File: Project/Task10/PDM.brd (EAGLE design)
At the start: 101.3 x 78.7 mm, 43 parts

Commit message: Final Board Revision
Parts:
- moved R1 6.35 mm to (73.7, 30.5)
- moved R2 6.35 mm to (73.7, 26.7)
- moved R3 6.35 mm to (73.7, 22.9)
- moved R4 6.35 mm to (73.7, 19.1)
- moved R5 6.35 mm to (73.7, 15.2)
- moved R6 6.35 mm to (73.7, 11.4)
- moved LED1 6.35 mm to (80.0, 30.5)
- moved LED2 6.35 mm to (80.0, 26.7)
- moved LED3 6.35 mm to (80.0, 22.9)
- moved LED4 6.35 mm to (80.0, 19.1)
- moved LED5 6.35 mm to (80.0, 15.2)
- moved LED6 6.35 mm to (80.0, 11.4)
- moved C9 1.27 mm to (82.5, 41.9)
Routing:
- net N$15: track 0.00 -> 71.0 mm, vias 0 -> 1
- net N$19: track 3.91 -> 66.0 mm, vias 0 -> 1
- net N$6: track 4.04 -> 57.6 mm, vias 0 -> 1
- net N$1: track 0.00 -> 51.6 mm, vias 0 -> 1
- net N$9: track 3.91 -> 55.5 mm, vias 0 -> 1
- net N$4: track 0.00 -> 42.2 mm, vias 0 -> 1
- net GND: track 36.3 -> 62.3 mm, vias 0 -> 3
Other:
- board size 101.3 x 78.7 mm -> 101.3 x 76.2 mm
- board text added: "Acc 1"
- board text added: "Acc 2"
- board text added: "Acc 3"
- board text added: "Arduino"
- board text added: "MRSD Team B, Fall 2013"
- board text added: "Power Status"
- board text added: "Rev 0.1"
- board text added: "Servo 1"
- board text added: "Servo 2"
- board text added: "Space Jockey Power Distribution Board"
- board text removed: "Power Distribution Board - Team Space Jockey"
- board text removed: "Status"

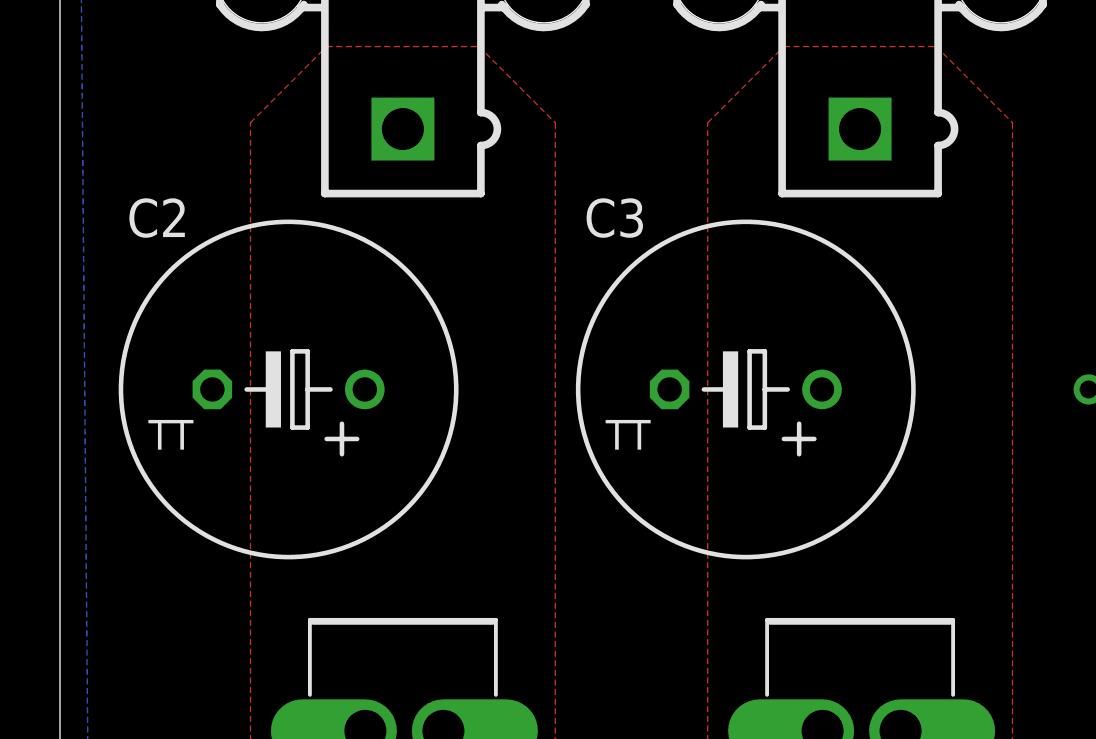
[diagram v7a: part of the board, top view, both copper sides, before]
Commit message: Final Board design.
Looks good. I just moved the giant capacitors one grid to the left to
enlarge the clearance with the ground
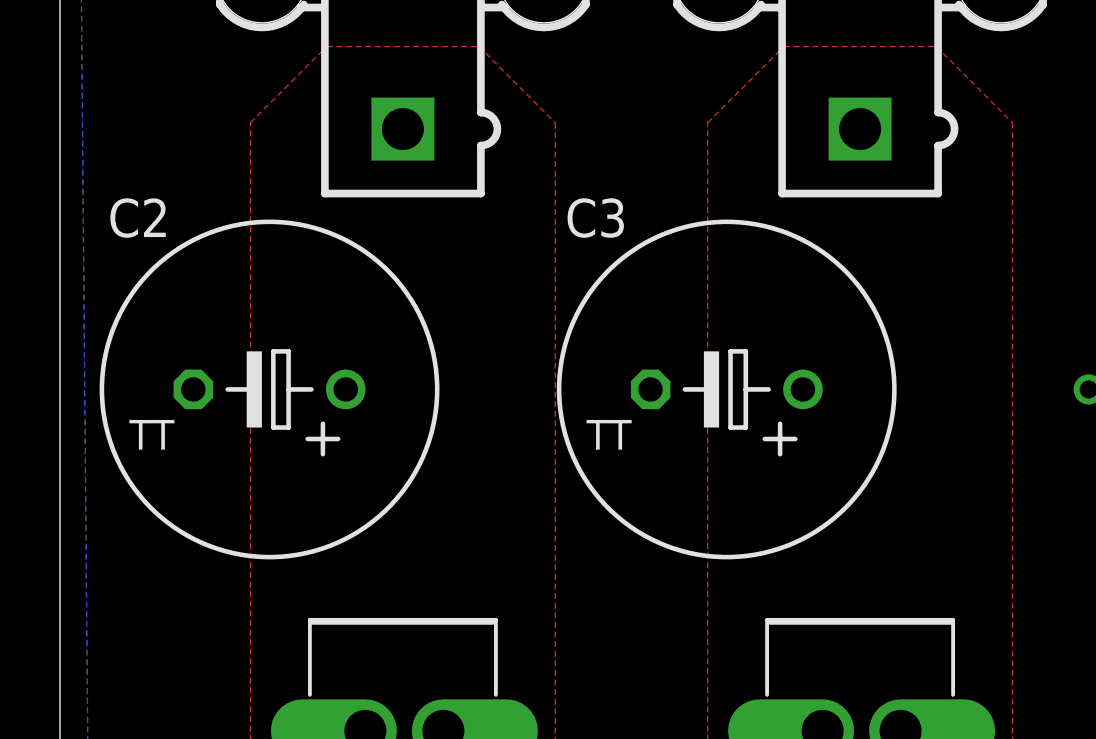
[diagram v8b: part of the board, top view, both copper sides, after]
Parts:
- moved C2 0.63 mm to (6.99, 53.3)
- moved C3 0.63 mm to (22.2, 53.3)
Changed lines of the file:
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@@
 <attribute name="OC_FARNELL" value="1822072" x="57.15" y="64.77" size="1.778" layer="27" display="off"/>
 </element>
-<element name="C2" library="rcl" package="TT5D11" value="" x="7.62" y="53.34" smashed="yes" rot="R180">
-<attribute name="NAME" x="4.318" y="59.69" size="1.27" layer="25" ratio="10" rot="R180"/>
-<attribute name="VALUE" x="11.303" y="56.769" size="1.27" layer="27" ratio="10" rot="R180"/>
+<element name="C2" library="rcl" package="TT5D11" value="" x="6.985" y="53.34" smashed="yes" rot="R180">
+<attribute name="NAME" x="3.683" y="59.69" size="1.27" layer="25" ratio="10" rot="R180"/>
+<attribute name="VALUE" x="10.668" y="56.769" size="1.27" layer="27" ratio="10" rot="R180"/>
 </element>
-<element name="C3" library="rcl" package="TT5D11" value="" x="22.86" y="53.34" smashed="yes" rot="R180">
-<attribute name="NAME" x="19.558" y="59.69" size="1.27" layer="25" ratio="10" rot="R180"/>
-<attribute name="VALUE" x="26.543" y="56.769" size="1.27" layer="27" ratio="10" rot="R180"/>
+<element name="C3" library="rcl" package="TT5D11" value="" x="22.225" y="53.34" smashed="yes" rot="R180">
+<attribute name="NAME" x="18.923" y="59.69" size="1.27" layer="25" ratio="10" rot="R180"/>
+<attribute name="VALUE" x="25.908" y="56.769" size="1.27" layer="27" ratio="10" rot="R180"/>
 </element>
 <element name="BATT1_W" library="MRSDTeamB" package="CON_XT60_PIGTAIL" value="" x="52.07" y="19.05" rot="R180"/>
